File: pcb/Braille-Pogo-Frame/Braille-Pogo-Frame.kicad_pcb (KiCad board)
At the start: 2 copper layers, 74 x 95 mm, 64 parts, among them J1 Conn_01x06, J10 Screw_Terminal_01x02, J2 Conn_01x06, J3 Conn_01x06, J4 Conn_01x06, J9 Conn_01x02, M1 Stepper_Motor_bipolar, M2 Stepper_Motor_bipolar, M3 Stepper_Motor_bipolar, M4 Stepper_Motor_bipolar, SW1 SW_Push, SW2 SW_Push, U1 DRV8847SPWR, U2 DRV8847SPWR, U3 DRV8847SPWR, U4 DRV8847SPWR, U9 RP2040-Zero

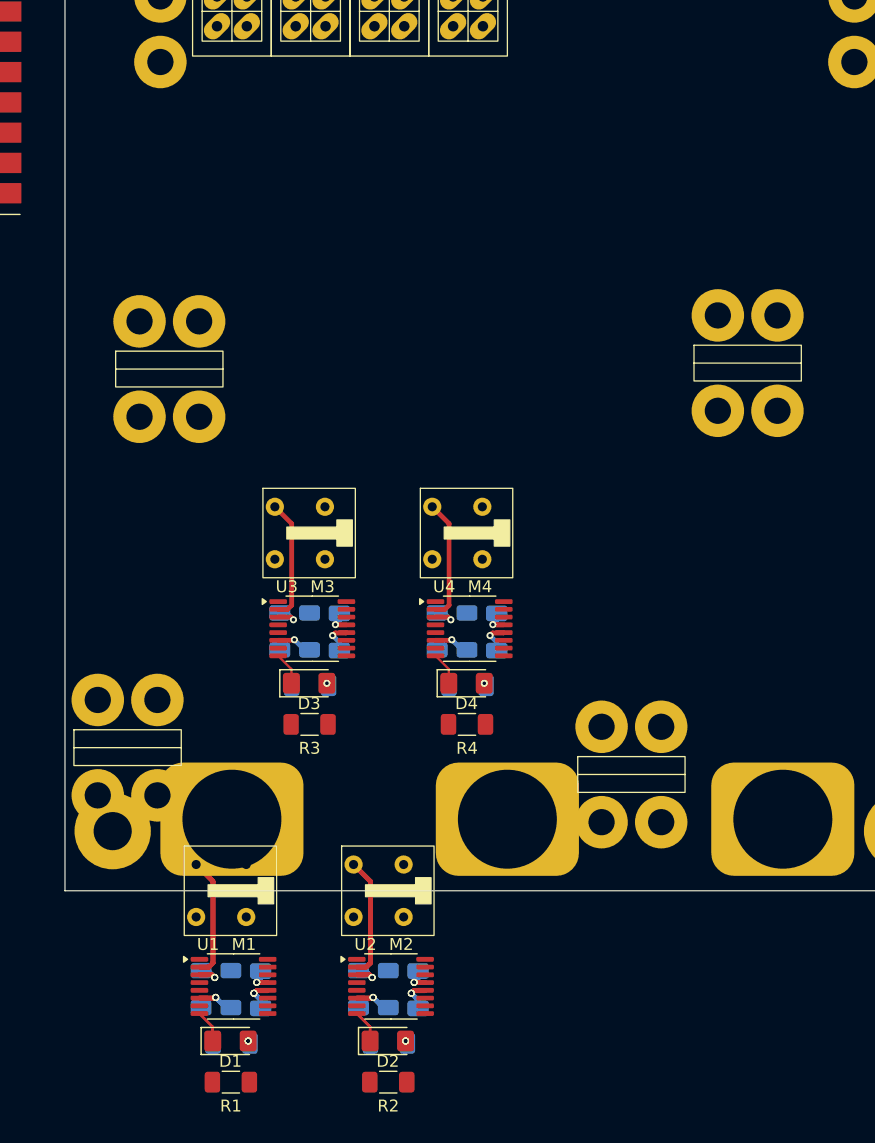
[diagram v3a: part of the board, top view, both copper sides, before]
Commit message: Create horizontal_bar_holder CAD
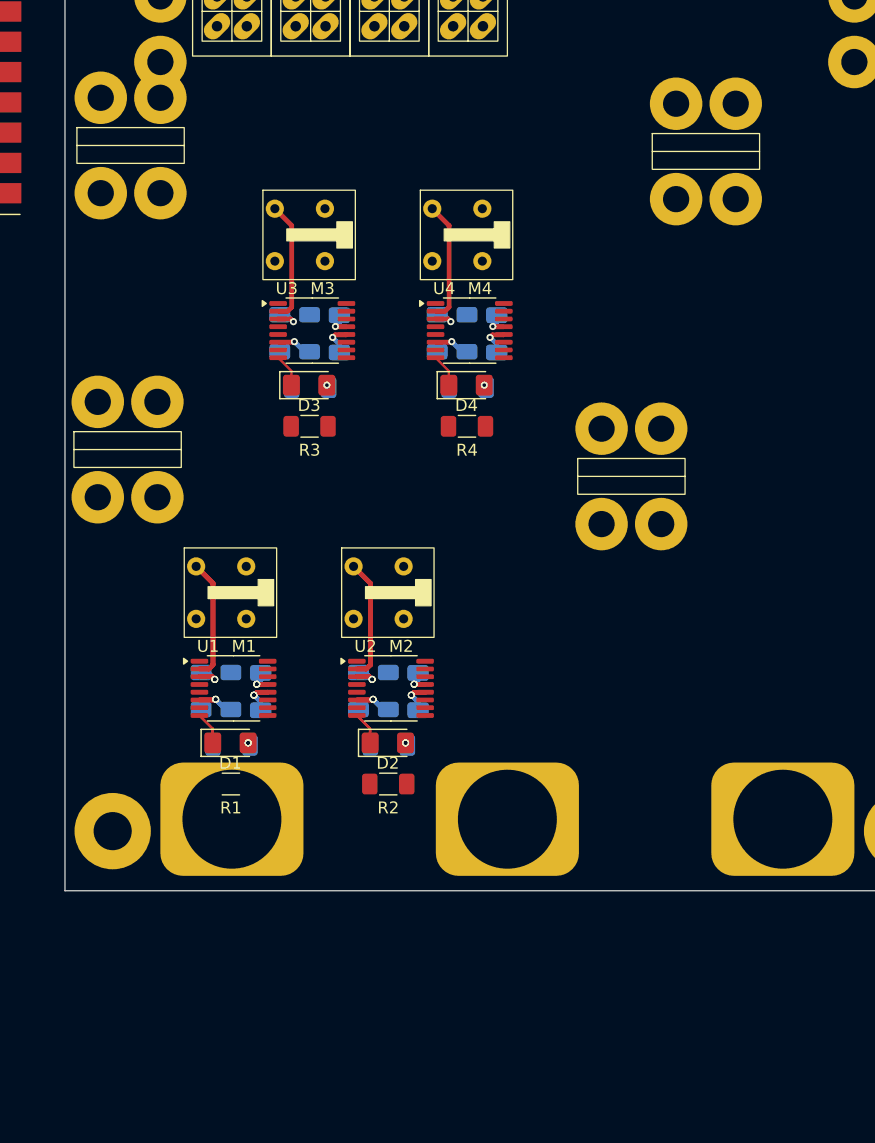
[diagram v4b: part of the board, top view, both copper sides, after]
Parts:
- moved C1 25.0 mm to (102.4, 158.3)
- moved C2 25.0 mm to (115.6, 158.3)
- moved C3 25.0 mm to (109.0, 128.3)
- moved C4 25.0 mm to (122.2, 128.3)
- moved D1 25.0 mm to (99.9, 162.6)
- moved D2 25.0 mm to (113.1, 162.6)
- moved D3 25.0 mm to (106.5, 132.6)
- moved D4 25.0 mm to (119.7, 132.6)
- moved H18 25.0 mm to (91.2, 138.0)
- moved H20 25.0 mm to (133.5, 140.2)
- moved M1 25.0 mm to (100.0, 150.0)
- moved M2 25.0 mm to (113.2, 150.0)
- moved M3 25.0 mm to (106.6, 120.0)
- moved M4 25.0 mm to (119.8, 120.0)
- moved R1 25.0 mm to (99.9, 166.1)
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
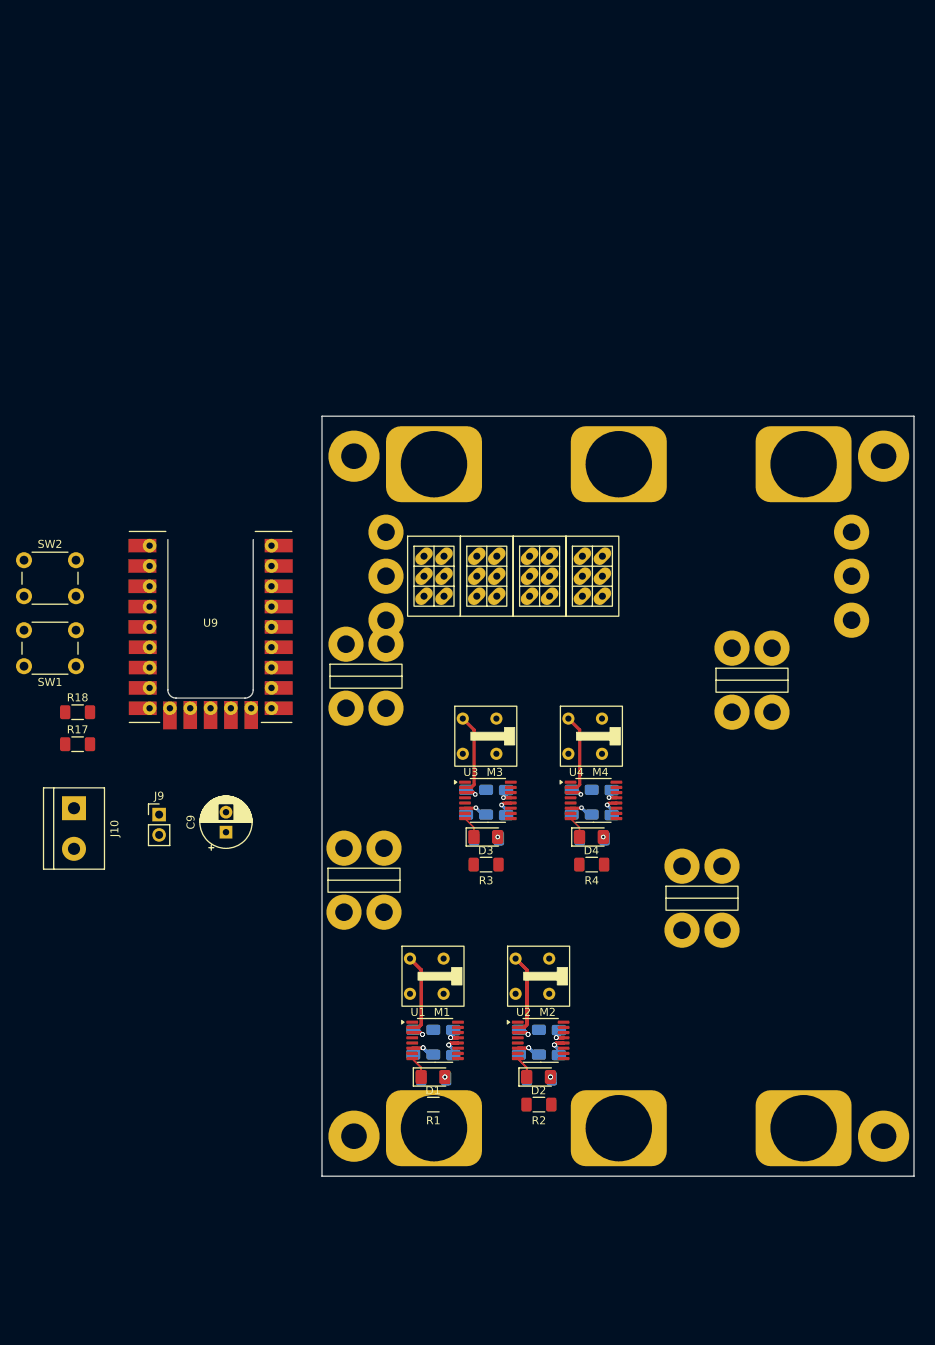
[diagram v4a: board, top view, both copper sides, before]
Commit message: Add horiz mounting standoffs, layout
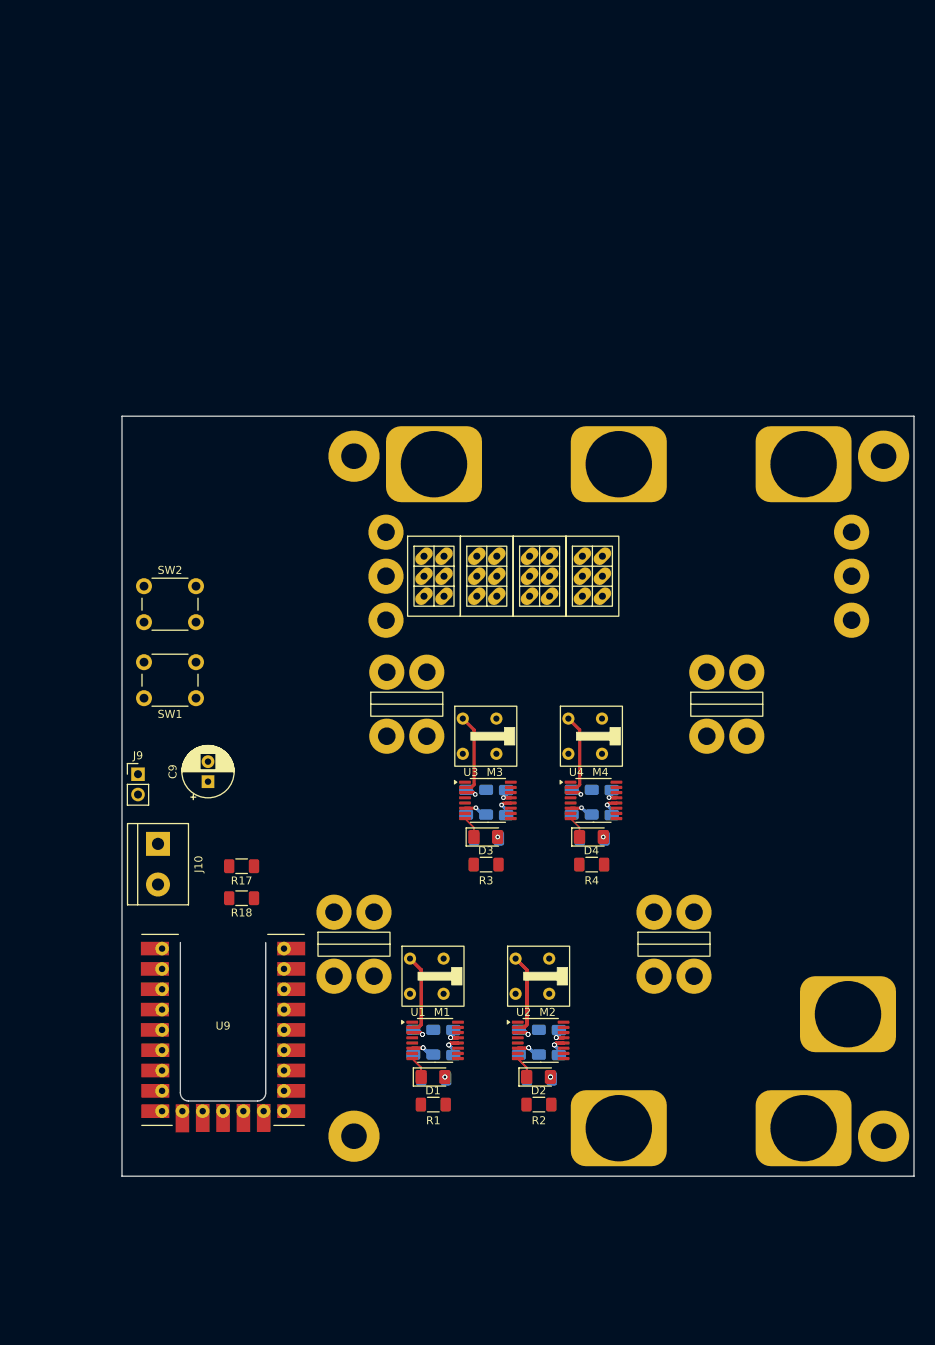
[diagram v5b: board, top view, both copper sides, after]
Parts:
- moved H4 53.7 mm to (151.8, 154.8)
- moved U9 50.4 mm to (63.5, 169.5)
- moved R18 31.0 mm to (76.0, 140.2), turned to 180 degrees
- moved R17 25.6 mm to (76.0, 136.2), turned to 180 degrees
- moved SW1 15.5 mm to (70.2, 115.2)
- moved SW2 15.3 mm to (63.8, 101.2)
- moved J10 11.4 mm to (65.5, 133.5)
- moved H18 8.10 mm to (90.0, 146.0)
- moved H20 6.73 mm to (130.0, 146.0)
- moved C9 6.71 mm to (71.8, 125.7)
- moved H17 6.19 mm to (96.6, 116.0)
- moved J9 5.70 mm to (63.0, 124.8)
- moved H19 4.35 mm to (136.6, 116.0)
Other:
- board size 74 x 95 mm -> 99 x 95 mm

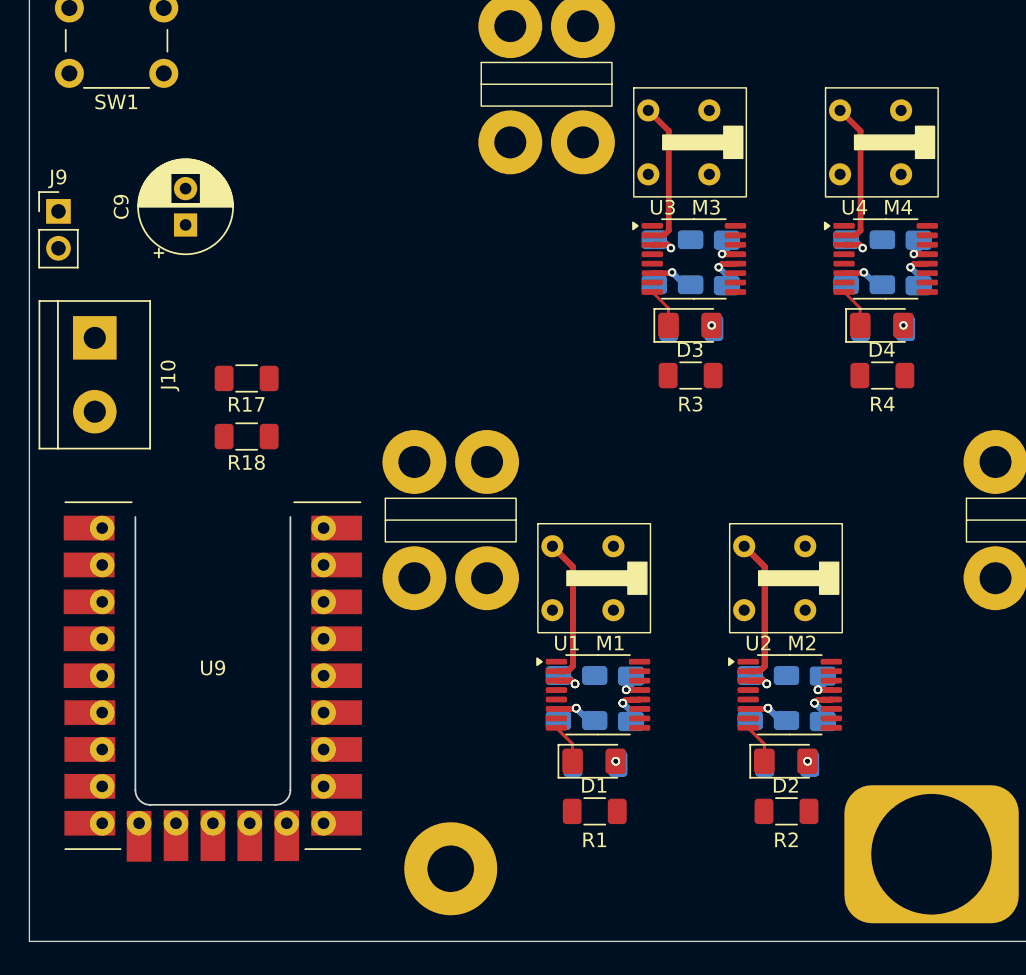
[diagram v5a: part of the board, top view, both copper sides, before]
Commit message: Create render of gear-based PCB in current state
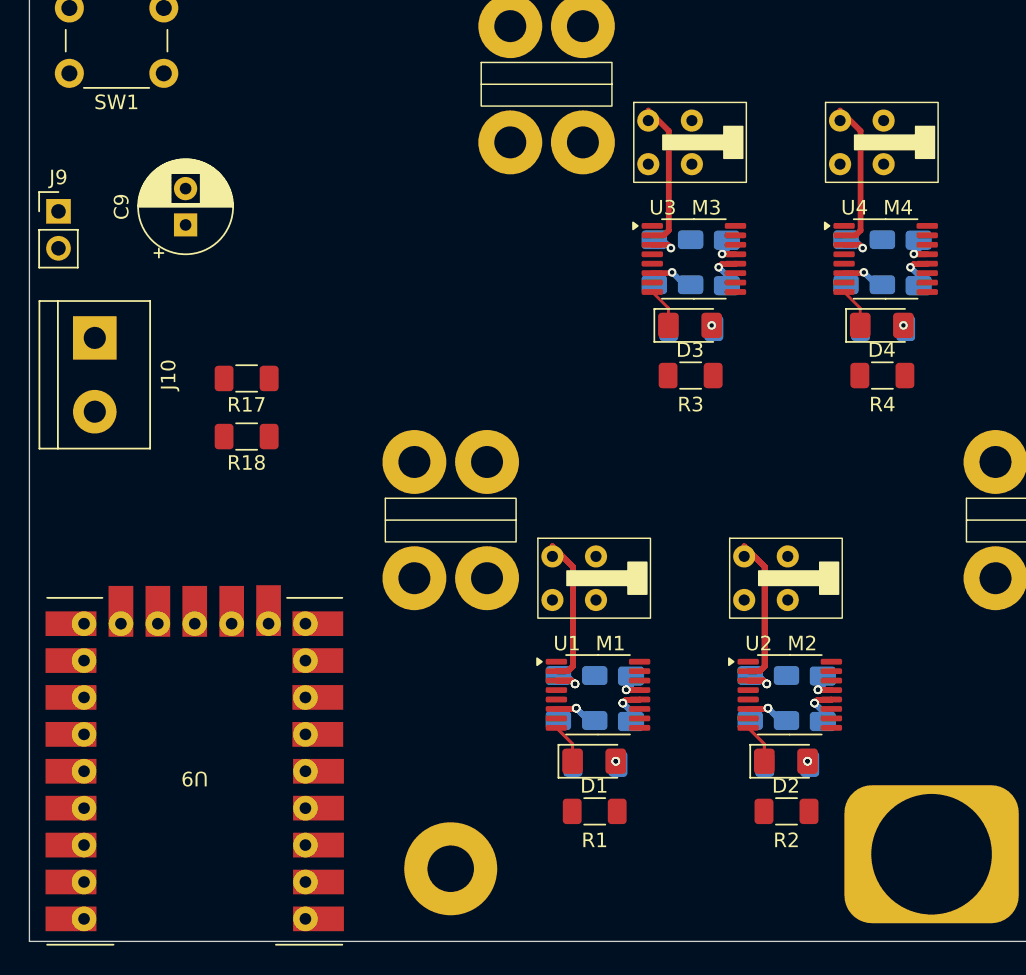
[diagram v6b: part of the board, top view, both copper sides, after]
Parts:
- moved U9 27.0 mm to (82.5, 150.5), turned to 180 degrees

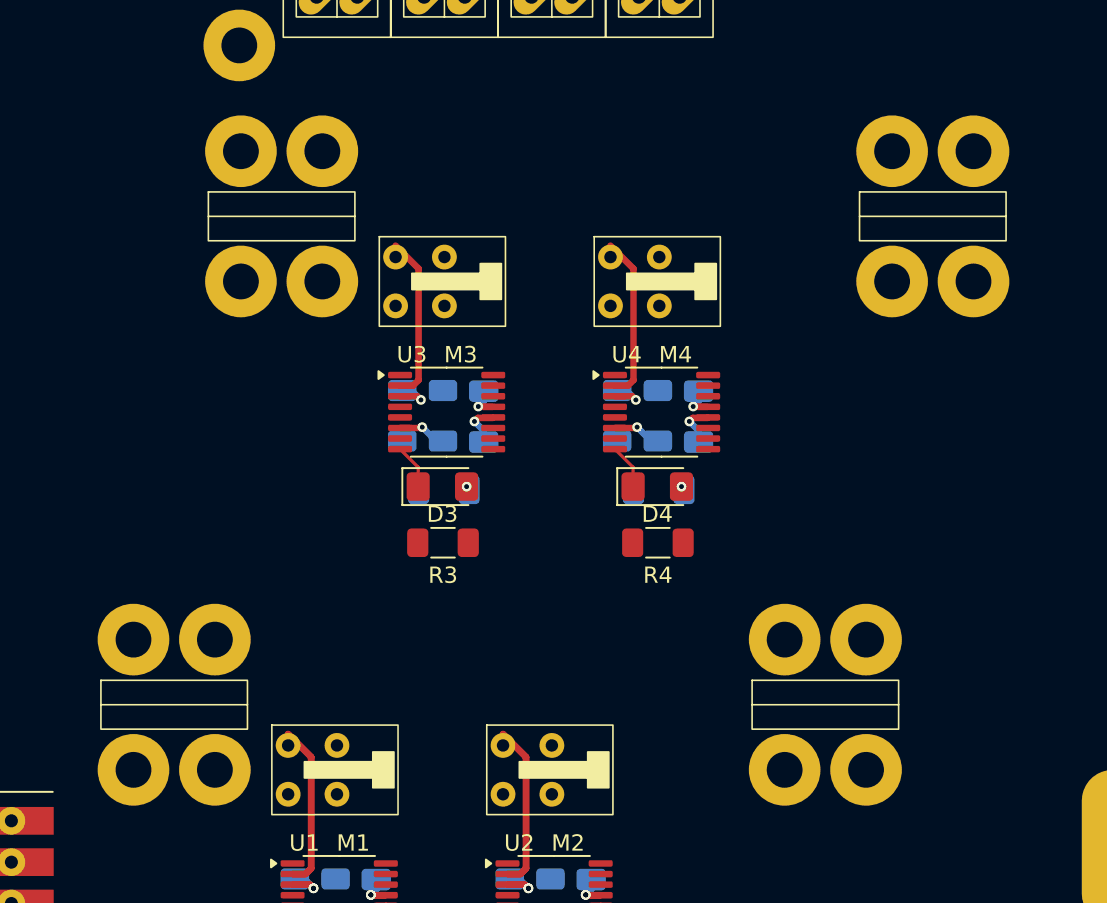
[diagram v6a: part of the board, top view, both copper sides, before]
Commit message: Update spool geometry so it fits
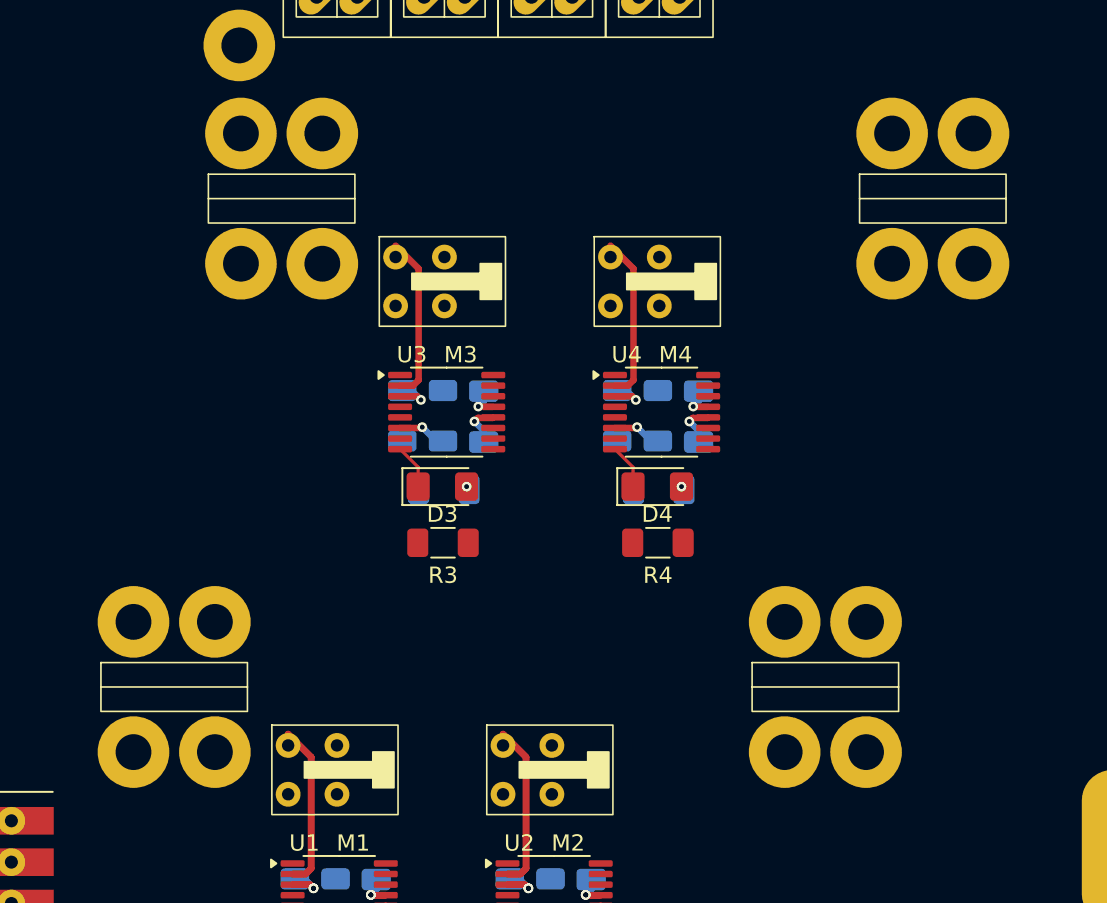
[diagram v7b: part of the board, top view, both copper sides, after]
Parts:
- moved H17 1.09 mm to (96.6, 114.9)
- moved H18 1.09 mm to (90.0, 144.9)
- moved H19 1.09 mm to (136.6, 114.9)
- moved H20 1.09 mm to (130.0, 144.9)
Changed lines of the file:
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@@
 	(footprint "00-lib-footprints:HorizMounting_4x_M2_and_M3_Middle"
 		(layer "F.Cu")
-		(at 136.6 116)
+		(at 136.6 114.91)
 		(descr "Mounting Hole 3.2mm, M3")
 		(tags "mounting hole 3.2mm m3")
@@
 		)
 		(property "Footprint" "00-lib-footprints:RP2040 Zero"
-			(at 0 0 360)
+			(at 0 0 0)
 			(layer "F.Fab")
 			(hide yes)
@@
 		)
 		(property "Datasheet" ""
-			(at 0 0 360)
+			(at 0 0 0)
 			(layer "F.Fab")
 			(hide yes)
@@
 		)
 		(property "Description" ""
-			(at 0 0 360)
+			(at 0 0 0)
 			(layer "F.Fab")
 			(hide yes)
@@
 	(footprint "00-lib-footprints:HorizMounting_4x_M2_and_M3_Middle"
 		(layer "F.Cu")
-		(at 90 146)
+		(at 90 144.91)
 		(descr "Mounting Hole 3.2mm, M3")
 		(tags "mounting hole 3.2mm m3")
@@
 	(footprint "00-lib-footprints:HorizMounting_4x_M2_and_M3_Middle"
 		(layer "F.Cu")
-		(at 130 146)
+		(at 130 144.91)
 		(descr "Mounting Hole 3.2mm, M3")
 		(tags "mounting hole 3.2mm m3")
@@
 	(footprint "00-lib-footprints:HorizMounting_4x_M2_and_M3_Middle"
 		(layer "F.Cu")
-		(at 96.6 116)
+		(at 96.6 114.91)
 		(descr "Mounting Hole 3.2mm, M3")
 		(tags "mounting hole 3.2mm m3")
